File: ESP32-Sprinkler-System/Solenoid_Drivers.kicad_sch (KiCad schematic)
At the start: 44 parts, among them J202 TBL004-508-02BE-2GY, J203 TBL004-508-02BE-2GY, J204 TBL004-508-02BE-2GY, Q202 IRFZ24NPBF, Q203 IRFZ24NPBF, Q204 IRFZ24NPBF, U201 MC33152PG, U202 MC33152PG

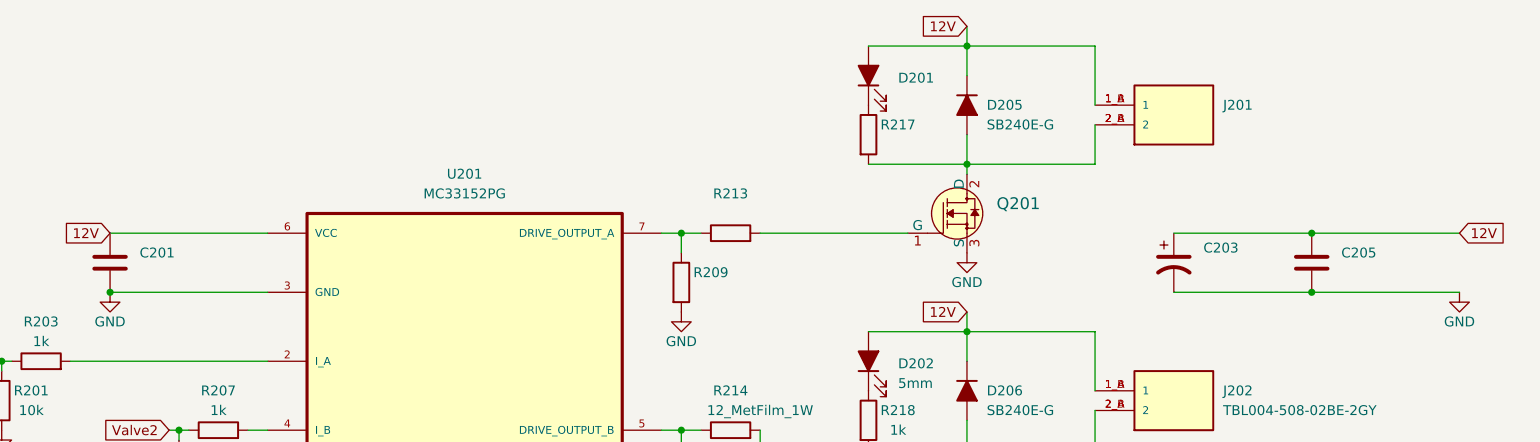
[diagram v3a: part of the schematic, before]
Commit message: Found symbol and footprint for ESP32 DevKit, schematic 80% done.
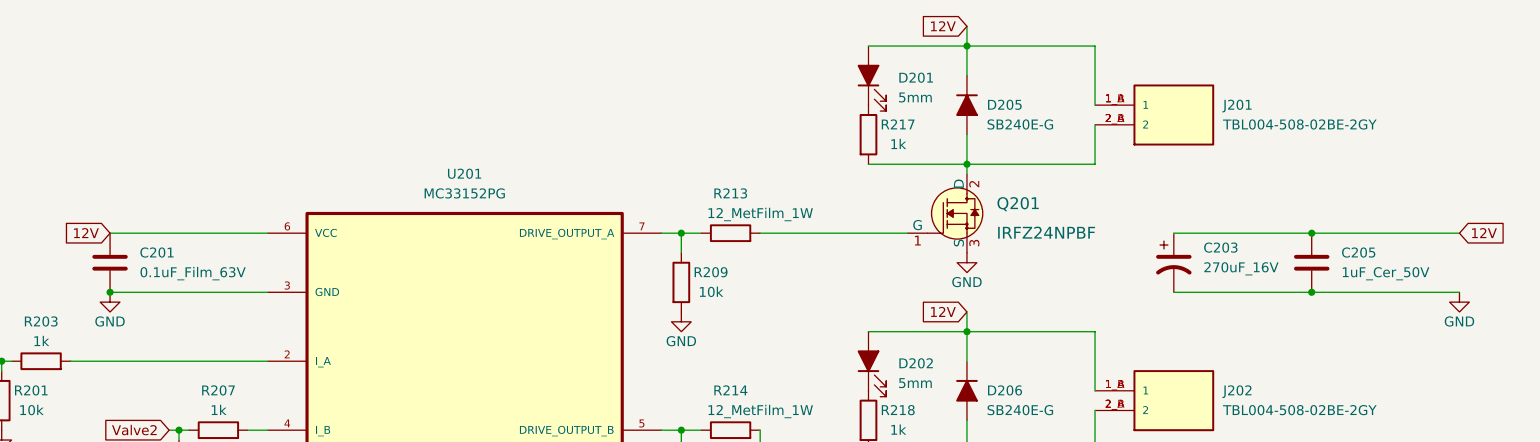
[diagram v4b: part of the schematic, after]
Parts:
- C201: value (none) -> 0.1uF_Film_63V; footprint (none) -> Capacitor_THT:C_Rect_L7.0mm_W2.5mm_P5.00mm
- C203: value (none) -> 270uF_16V; footprint (none) -> Capacitor_THT:CP_Radial_D6.3mm_P2.50mm
- C205: value (none) -> 1uF_Cer_50V; footprint (none) -> Capacitor_THT:C_Disc_D7.5mm_W4.4mm_P5.00mm
- D201: value (none) -> 5mm; footprint (none) -> LED_THT:LED_D5.0mm
- J201: value (none) -> TBL004-508-02BE-2GY; footprint (none) -> TBL004-508-02BE-2GY:CUI_TBL004-508-02BE-2GY
- Q201: value (none) -> IRFZ24NPBF; footprint (none) -> Package_TO_SOT_THT:TO-220-3_Vertical
- R209: value (none) -> 10k
- R213: value (none) -> 12_MetFilm_1W; footprint (none) -> Resistor_THT:R_Axial_DIN0207_L6.3mm_D2.5mm_P10.16mm_Horizontal
- R217: value (none) -> 1k
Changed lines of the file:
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@@
       (effects (font (size 1.27 1.27)) (justify left))
     )
-    (property "Value" "" (id 1) (at 193.04 48.8949 0)
-      (effects (font (size 1.27 1.27)) (justify left))
-    )
-    (property "Footprint" "" (id 2) (at 189.23 48.26 0)
+    (property "Value" "270uF_16V" (id 1) (at 193.04 48.8949 0)
+      (effects (font (size 1.27 1.27)) (justify left))
+    )
+    (property "Footprint" "Capacitor_THT:CP_Radial_D6.3mm_P2.50mm" (id 2) (at 189.23 48.26 0)
       (effects (font (size 1.27 1.27)) hide)
     )
@@
       (effects (font (size 1.27 1.27)) (justify left))
     )
-    (property "Value" "" (id 1) (at 210.82 49.5299 0)
-      (effects (font (size 1.27 1.27)) (justify left))
-    )
-    (property "Footprint" "" (id 2) (at 207.9752 52.07 0)
+    (property "Value" "1uF_Cer_50V" (id 1) (at 210.82 49.5299 0)
+      (effects (font (size 1.27 1.27)) (justify left))
+    )
+    (property "Footprint" "Capacitor_THT:C_Disc_D7.5mm_W4.4mm_P5.00mm" (id 2) (at 207.9752 52.07 0)
       (effects (font (size 1.27 1.27)) hide)
     )
@@
       (effects (font (size 1.524 1.524)) (justify left))
     )
-    (property "Value" "" (id 1) (at 166.37 44.45 0)
+    (property "Value" "IRFZ24NPBF" (id 1) (at 166.37 44.45 0)
       (effects (font (size 1.524 1.524)) (justify left))
     )
-    (property "Footprint" "" (id 2) (at 167.64 36.83 0)
+    (property "Footprint" "Package_TO_SOT_THT:TO-220-3_Vertical" (id 2) (at 167.64 36.83 0)
       (effects (font (size 1.524 1.524)) (justify left) hide)
     )
@@
       (effects (font (size 1.27 1.27)) hide)
     )
-    (pin "2")
-    (pin "1")
+    (pin "1")
+    (pin "2")
   )
   (symbol (lib_id "Device:R") (at 60.96 74.93 0) (unit 1)
@@
       (effects (font (size 1.27 1.27)) (justify left))
     )
-    (property "Value" "" (id 1) (at 195.58 30.4799 0)
-      (effects (font (size 1.27 1.27)) (justify left))
-    )
-    (property "Footprint" "" (id 2) (at 189.23 30.48 0)
+    (property "Value" "TBL004-508-02BE-2GY" (id 1) (at 195.58 30.4799 0)
+      (effects (font (size 1.27 1.27)) (justify left))
+    )
+    (property "Footprint" "TBL004-508-02BE-2GY:CUI_TBL004-508-02BE-2GY" (id 2) (at 189.23 30.48 0)
       (effects (font (size 1.27 1.27)) (justify left bottom) hide)
     )
@@
     (in_bom yes) (on_board yes)
     (property "Reference" "R217" (id 0) (at 153.67 30.48 0))
-    (property "Value" "" (id 1) (at 153.67 33.02 0))
+    (property "Value" "1k" (id 1) (at 153.67 33.02 0))
     (property "Footprint" "Resistor_THT:R_Axial_DIN0207_L6.3mm_D2.5mm_P10.16mm_Horizontal" (id 2) (at 148.082 31.75 90)
       (effects (font (size 1.27 1.27)) hide)
@@
     (in_bom yes) (on_board yes)
     (property "Reference" "R213" (id 0) (at 132.08 39.37 90))
-    (property "Value" "" (id 1) (at 135.89 41.91 90))
-    (property "Footprint" "" (id 2) (at 132.08 46.228 90)
+    (property "Value" "12_MetFilm_1W" (id 1) (at 135.89 41.91 90))
+    (property "Footprint" "Resistor_THT:R_Axial_DIN0207_L6.3mm_D2.5mm_P10.16mm_Horizontal" (id 2) (at 132.08 46.228 90)
       (effects (font (size 1.27 1.27)) hide)
     )
@@
     (in_bom yes) (on_board yes)
     (property "Reference" "R209" (id 0) (at 129.54 49.53 0))
-    (property "Value" "" (id 1) (at 129.54 52.07 0))
+    (property "Value" "10k" (id 1) (at 129.54 52.07 0))
     (property "Footprint" "Resistor_THT:R_Axial_DIN0207_L6.3mm_D2.5mm_P10.16mm_Horizontal" (id 2) (at 123.952 50.8 90)
       (effects (font (size 1.27 1.27)) hide)
@@
       (effects (font (size 1.27 1.27)) (justify right))
     )
-    (property "Value" "" (id 1) (at 153.67 26.9874 90)
+    (property "Value" "5mm" (id 1) (at 153.67 26.9874 90)
       (effects (font (size 1.27 1.27)) (justify right))
     )
-    (property "Footprint" "" (id 2) (at 149.86 24.13 0)
+    (property "Footprint" "LED_THT:LED_D5.0mm" (id 2) (at 149.86 24.13 0)
       (effects (font (size 1.27 1.27)) hide)
     )
@@
       (effects (font (size 1.27 1.27)) (justify left))
     )
-    (property "Value" "" (id 1) (at 55.88 49.5299 0)
-      (effects (font (size 1.27 1.27)) (justify left))
-    )
-    (property "Footprint" "" (id 2) (at 53.0352 52.07 0)
-      (effects (font (size 1.27 1.27)) hide)
-    )
+    (property "Value" "0.1uF_Film_63V" (id 1) (at 55.88 49.5299 0)
+      (effects (font (size 1.27 1.27)) (justify left))
+    )
+    (property "Footprint" "Capacitor_THT:C_Rect_L7.0mm_W2.5mm_P5.00mm" (id 2) (at 53.0352 52.07 0)
+      (effects (font (size 1.27 1.27)) hide)
+    )

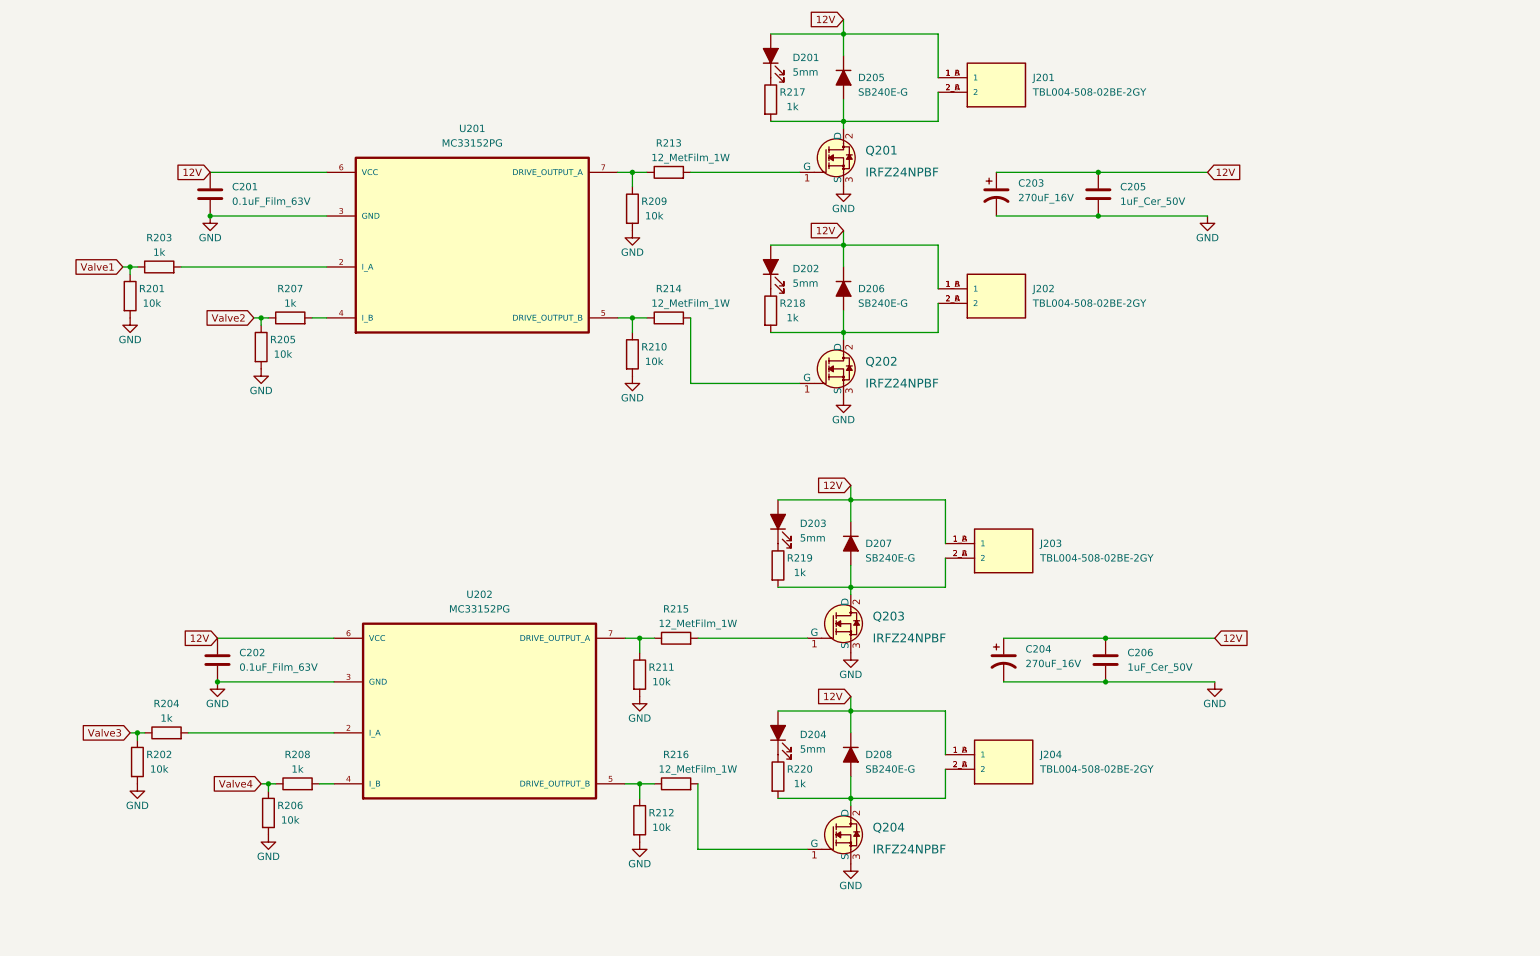
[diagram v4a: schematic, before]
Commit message: Schematic done, footprints assigned, terminal block requires footprint clarity, some 3D models missing.
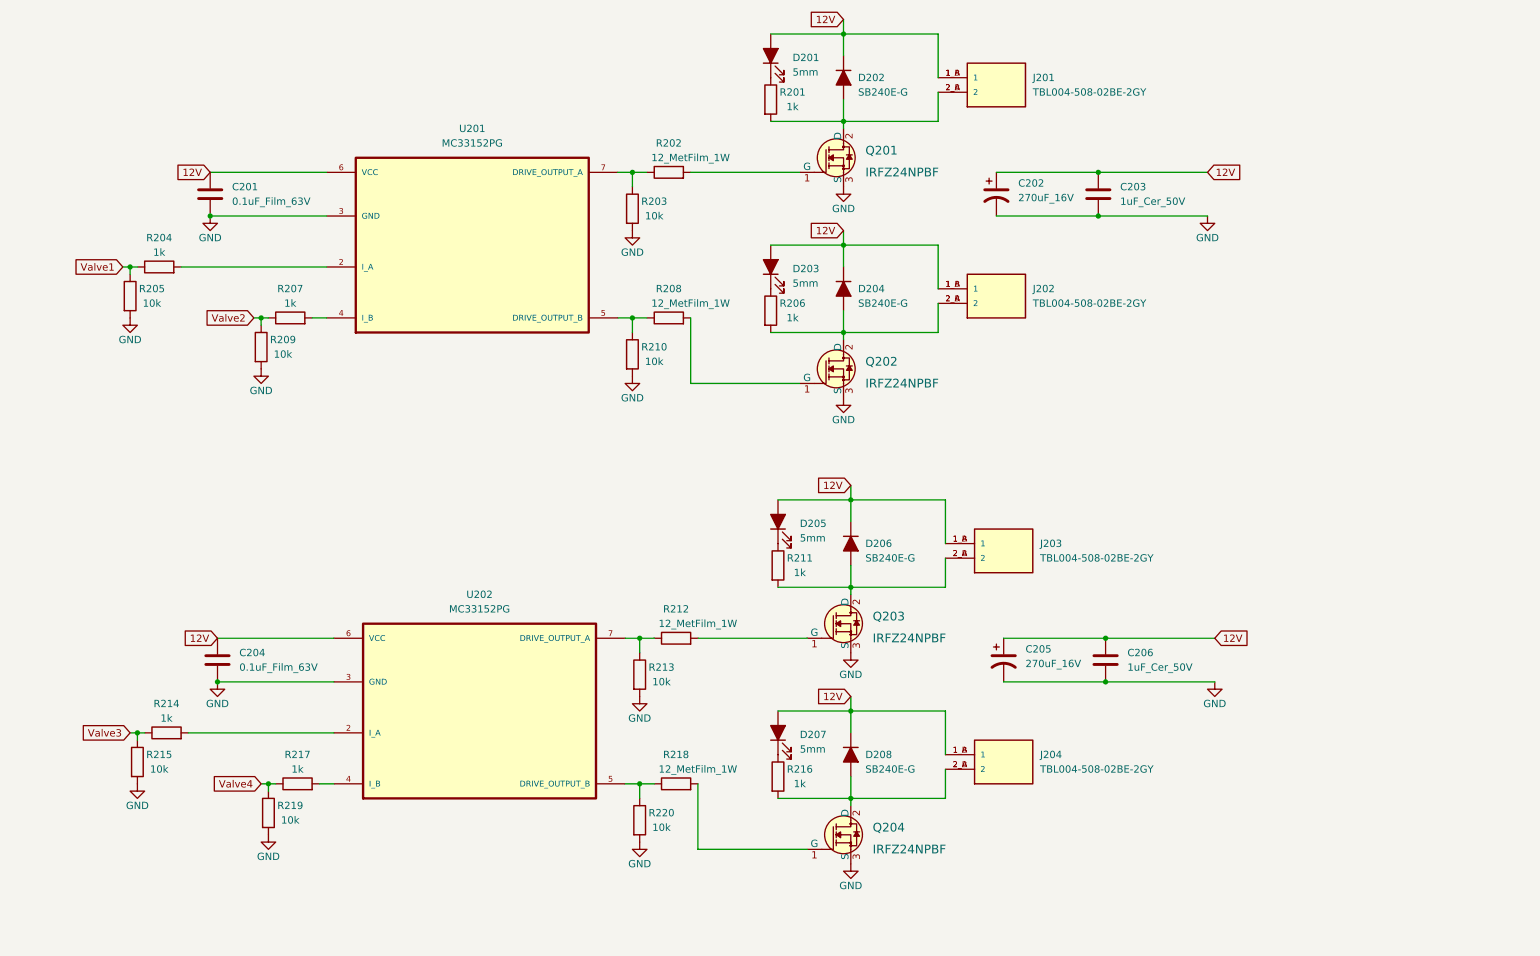
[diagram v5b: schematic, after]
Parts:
- renumbered C203 to C202, C205 to C203, C202 to C204, C204 to C205, D205 to D202, D202 to D203, D206 to D204, D203 to D205, D207 to D206, D204 to D207, R217 to R201, R213 to R202, R209 to R203, R203 to R204, R201 to R205, R218 to R206, R214 to R208, R205 to R209, R219 to R211, R215 to R212, R211 to R213, R204 to R214, R202 to R215, R220 to R216, R208 to R217, R216 to R218, R206 to R219, R212 to R220

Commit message: going to edit tracks
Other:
- note added: "Valve 1"
- note added: "Valve 2"
- note added: "Valve 3"
- note added: "Valve 4"
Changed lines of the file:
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@@
     (stroke (width 0) (type default) (color 0 0 0 0))
+  )
+  (text "Valve 2" (at 242.57 66.04 0)
+    (effects (font (size 1.27 1.27)) (justify left bottom))
+  )
+  (text "Valve 4" (at 245.11 148.59 0)
+    (effects (font (size 1.27 1.27)) (justify left bottom))
+  )
+  (text "Valve 1" (at 242.57 31.75 0)
+    (effects (font (size 1.27 1.27)) (justify left bottom))
+  )
+  (text "Valve 3" (at 243.84 111.76 0)
+    (effects (font (size 1.27 1.27)) (justify left bottom))
   )
   (global_label "Valve2" (shape input) (at 59.69 69.85 180) (fields_autoplaced)
